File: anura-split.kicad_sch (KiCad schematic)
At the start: 41 parts, among them U1 Nice_Nano_V2

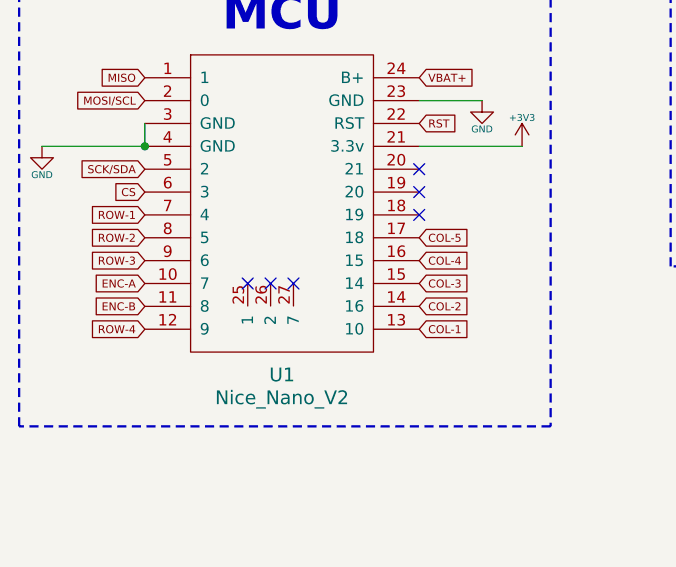
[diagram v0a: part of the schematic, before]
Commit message: lib-anura updates
added and updated variety of symbols in schematic library, to get rid of
dependencies
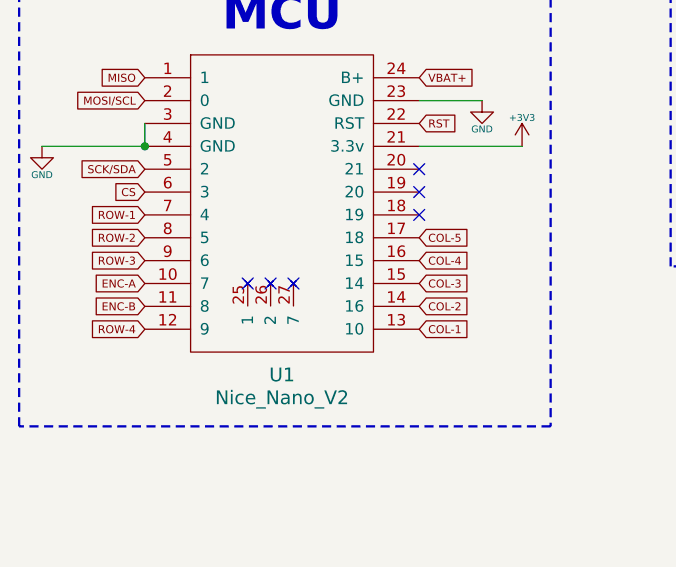
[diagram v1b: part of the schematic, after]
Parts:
- D-1, D-10, D-11, D-12, D-13, D-14, D-15, D-16, D-17, D-18, D-2, D-3, D-4, D-5, D-6, D-7, D-8, D-9: symbol ScottoKeebs:Placeholder_Diode -> lib-anura:Diode_SOD123
- DS-L-1: symbol lib-chungus:Nice!View -> lib-anura:Nice!View
- SW-1, SW-10, SW-11, SW-12, SW-13, SW-14, SW-15, SW-16, SW-17, SW-2, SW-3, SW-4, SW-5, SW-6, SW-7, SW-8, SW-9: symbol ScottoKeebs:Placeholder_Keyswitch -> lib-anura:SW_Push_45_Deg
- SW-BAT-1: symbol Switch:SW_SPDT -> lib-anura:SW_SPDT
- SW-RST-L1: symbol Switch:SW_Push -> lib-anura:SW_Push
- U1: symbol ScottoKeebs:MCU_Nice_Nano_V2 -> lib-anura:MCU_Nice_Nano_V2
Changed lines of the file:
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@@
 	)
 	(symbol
-		(lib_id "ScottoKeebs:Placeholder_Keyswitch")
+		(lib_id "lib-anura:SW_Push_45_Deg")
 		(at 168.275 60.325 0)
 		(unit 1)
@@
 	)
 	(symbol
-		(lib_id "ScottoKeebs:Placeholder_Keyswitch")
+		(lib_id "lib-anura:SW_Push_45_Deg")
 		(at 186.055 79.375 0)
 		(unit 1)
@@
 	)
 	(symbol
-		(lib_id "ScottoKeebs:Placeholder_Diode")
+		(lib_id "lib-anura:Diode_SOD123")
 		(at 224.155 85.725 90)
 		(unit 1)
@@
 	)
 	(symbol
-		(lib_id "ScottoKeebs:Placeholder_Diode")
+		(lib_id "lib-anura:Diode_SOD123")
 		(at 206.375 85.725 90)
 		(unit 1)
@@
 	)
 	(symbol
-		(lib_id "ScottoKeebs:Placeholder_Keyswitch")
+		(lib_id "lib-anura:SW_Push_45_Deg")
 		(at 239.395 79.375 0)
 		(unit 1)
@@
 	)
 	(symbol
-		(lib_id "ScottoKeebs:Placeholder_Keyswitch")
+		(lib_id "lib-anura:SW_Push_45_Deg")
 		(at 221.615 60.325 0)
 		(unit 1)
@@
 	)
 	(symbol
-		(lib_id "ScottoKeebs:Placeholder_Keyswitch")
+		(lib_id "lib-anura:SW_Push_45_Deg")
 		(at 203.835 79.375 0)
 		(unit 1)
@@
 	)
 	(symbol
-		(lib_id "ScottoKeebs:Placeholder_Keyswitch")
+		(lib_id "lib-anura:SW_Push_45_Deg")
 		(at 168.275 79.375 0)
 		(unit 1)
@@
 	)
 	(symbol
-		(lib_id "ScottoKeebs:Placeholder_Diode")
+		(lib_id "lib-anura:Diode_SOD123")
 		(at 188.595 66.675 90)
 		(unit 1)
@@
 	)
 	(symbol
-		(lib_id "ScottoKeebs:Placeholder_Diode")
+		(lib_id "lib-anura:Diode_SOD123")
 		(at 224.155 104.775 90)
 		(unit 1)
@@
 	)
 	(symbol
-		(lib_id "ScottoKeebs:Placeholder_Diode")
+		(lib_id "lib-anura:Diode_SOD123")
 		(at 241.935 85.725 90)
 		(unit 1)
@@
 	)
 	(symbol
-		(lib_id "ScottoKeebs:MCU_Nice_Nano_V2")
+		(lib_id "lib-anura:MCU_Nice_Nano_V2")
 		(at 52.07 44.45 0)
 		(unit 1)
@@
 	)
 	(symbol
-		(lib_id "ScottoKeebs:Placeholder_Diode")
+		(lib_id "lib-anura:Diode_SOD123")
 		(at 241.935 66.675 90)
 		(unit 1)
@@
 	)
 	(symbol
-		(lib_id "ScottoKeebs:Placeholder_Diode")
+		(lib_id "lib-anura:Diode_SOD123")
 		(at 188.595 47.625 90)
 		(unit 1)
@@
 	)
 	(symbol
-		(lib_id "Switch:SW_Push")
+		(lib_id "lib-anura:SW_Push")
 		(at 116.205 74.93 0)
 		(unit 1)
@@
 	)
 	(symbol
-		(lib_id "ScottoKeebs:Placeholder_Diode")
+		(lib_id "lib-anura:Diode_SOD123")
 		(at 206.375 47.625 90)
 		(unit 1)
@@
 	)
 	(symbol
-		(lib_id "ScottoKeebs:Placeholder_Keyswitch")
+		(lib_id "lib-anura:SW_Push_45_Deg")
 		(at 239.395 98.425 0)
 		(unit 1)
@@
 	)
 	(symbol
-		(lib_id "ScottoKeebs:Placeholder_Diode")
+		(lib_id "lib-anura:Diode_SOD123")
 		(at 224.155 47.625 90)
 		(unit 1)
@@
 	)
 	(symbol
-		(lib_id "ScottoKeebs:Placeholder_Keyswitch")
+		(lib_id "lib-anura:SW_Push_45_Deg")
 		(at 221.615 98.425 0)
 		(unit 1)
@@
 	)
 	(symbol
-		(lib_id "ScottoKeebs:Placeholder_Diode")
+		(lib_id "lib-anura:Diode_SOD123")
 		(at 170.815 47.625 90)
 		(unit 1)
@@
 	)
 	(symbol
-		(lib_id "ScottoKeebs:Placeholder_Diode")
+		(lib_id "lib-anura:Diode_SOD123")
 		(at 224.155 66.675 90)
 		(unit 1)
@@
 	)
 	(symbol
-		(lib_id "lib-chungus:Nice!View")
+		(lib_id "lib-anura:Nice!View")
 		(at 121.92 104.14 0)
 		(unit 1)
@@
 	)
 	(symbol
-		(lib_id "ScottoKeebs:Placeholder_Diode")
+		(lib_id "lib-anura:Diode_SOD123")
 		(at 241.935 104.775 90)
 		(unit 1)
@@
 	)
 	(symbol
-		(lib_id "ScottoKeebs:Placeholder_Keyswitch")
+		(lib_id "lib-anura:SW_Push_45_Deg")
 		(at 186.055 60.325 0)
 		(unit 1)
@@
 	)
 	(symbol
-		(lib_id "ScottoKeebs:Placeholder_Keyswitch")
+		(lib_id "lib-anura:SW_Push_45_Deg")
 		(at 239.395 60.325 0)
 		(unit 1)
@@
 	)
 	(symbol
-		(lib_id "ScottoKeebs:Placeholder_Diode")
+		(lib_id "lib-anura:Diode_SOD123")
 		(at 206.375 104.775 90)
 		(unit 1)
@@
 	)
 	(symbol
-		(lib_id "ScottoKeebs:Placeholder_Keyswitch")
+		(lib_id "lib-anura:SW_Push_45_Deg")
 		(at 186.055 41.275 0)
 		(unit 1)
@@
 	)
 	(symbol
-		(lib_id "ScottoKeebs:Placeholder_Keyswitch")
+		(lib_id "lib-anura:SW_Push_45_Deg")
 		(at 203.835 60.325 0)
 		(unit 1)
@@
 	)
 	(symbol
-		(lib_id "ScottoKeebs:Placeholder_Diode")
+		(lib_id "lib-anura:Diode_SOD123")
 		(at 241.935 47.625 90)
 		(unit 1)
@@
 	)
 	(symbol
-		(lib_id "ScottoKeebs:Placeholder_Keyswitch")
+		(lib_id "lib-anura:SW_Push_45_Deg")
 		(at 203.835 41.275 0)
 		(unit 1)
@@
 	)
 	(symbol
-		(lib_id "ScottoKeebs:Placeholder_Keyswitch")
+		(lib_id "lib-anura:SW_Push_45_Deg")
 		(at 168.275 41.275 0)
 		(unit 1)
@@
 	)
 	(symbol
-		(lib_id "ScottoKeebs:Placeholder_Keyswitch")
+		(lib_id "lib-anura:SW_Push_45_Deg")
 		(at 239.395 41.275 0)
 		(unit 1)
@@
 	)
 	(symbol
-		(lib_id "ScottoKeebs:Placeholder_Keyswitch")
+		(lib_id "lib-anura:SW_Push_45_Deg")
 		(at 221.615 41.275 0)
 		(unit 1)
@@
 	)
 	(symbol
-		(lib_id "ScottoKeebs:Placeholder_Diode")
+		(lib_id "lib-anura:Diode_SOD123")
 		(at 206.375 66.675 90)
 		(unit 1)
@@
 	)
 	(symbol
-		(lib_id "ScottoKeebs:Placeholder_Keyswitch")
+		(lib_id "lib-anura:SW_Push_45_Deg")
 		(at 221.615 79.375 0)
 		(unit 1)
@@
 	)
 	(symbol
-		(lib_id "ScottoKeebs:Placeholder_Diode")
+		(lib_id "lib-anura:Diode_SOD123")
 		(at 188.595 85.725 90)
 		(unit 1)
@@
 	)
 	(symbol
-		(lib_id "Switch:SW_SPDT")
+		(lib_id "lib-anura:SW_SPDT")
 		(at 120.65 36.83 0)
 		(unit 1)
@@
 	)
 	(symbol
-		(lib_id "ScottoKeebs:Placeholder_Diode")
+		(lib_id "lib-anura:Diode_SOD123")
 		(at 170.815 85.725 90)
 		(unit 1)
@@
 	)
 	(symbol
-		(lib_id "ScottoKeebs:Placeholder_Diode")
+		(lib_id "lib-anura:Diode_SOD123")
 		(at 170.815 66.675 90)
 		(unit 1)

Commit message: trace routing + silkscreen design
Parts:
- DS-1: renamed from DS-L-1; footprint anura:nice!view -> anura:nice!view_rev2
- renumbered SW-BAT-1 to SW-BAT1, SW-RST-L1 to SW-RST1
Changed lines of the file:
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@@
 		(dnp no)
 		(fields_autoplaced yes)
-		(property "Reference" "SW-RST-L1"
+		(property "Reference" "SW-RST1"
 			(at 116.205 67.31 0)
 			(effects
@@
 			(project "anura-split"
 				(path "/2f4d8bfb-914e-4eb2-88ea-03268c6fd720"
-					(reference "SW-RST-L1")
+					(reference "SW-RST1")
 					(unit 1)
 				)
@@
 		(on_board yes)
 		(dnp no)
-		(property "Reference" "DS-L-1"
+		(property "Reference" "DS-1"
 			(at 121.793 93.218 0)
 			(effects
@@
 			)
 		)
-		(property "Footprint" "anura:nice!view"
+		(property "Footprint" "anura:nice!view_rev2"
 			(at 121.92 104.14 0)
 			(effects
@@
 			(project "anura-split"
 				(path "/2f4d8bfb-914e-4eb2-88ea-03268c6fd720"
-					(reference "DS-L-1")
+					(reference "DS-1")
 					(unit 1)
 				)
@@
 		(on_board yes)
 		(dnp no)
-		(property "Reference" "SW-BAT-1"
+		(property "Reference" "SW-BAT1"
 			(at 120.65 28.702 0)
 			(effects
@@
 			(project "anura-split"
 				(path "/2f4d8bfb-914e-4eb2-88ea-03268c6fd720"
-					(reference "SW-BAT-1")
-					(unit 1)
-				)
+					(reference "SW-BAT1")
+					(unit 1)
+				)

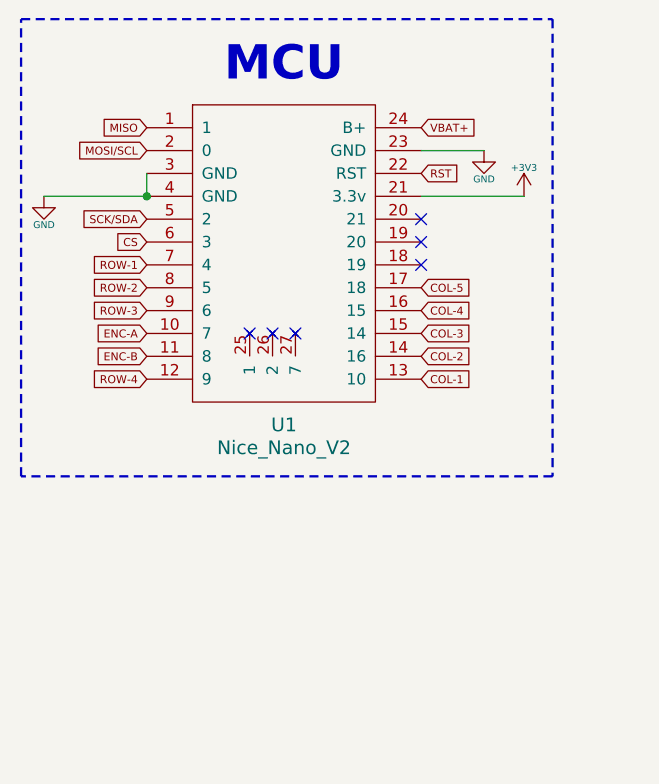
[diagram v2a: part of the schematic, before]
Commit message: routing + schematic changes
mcu nets reorganised to suit trace routing better, and more traces
routed
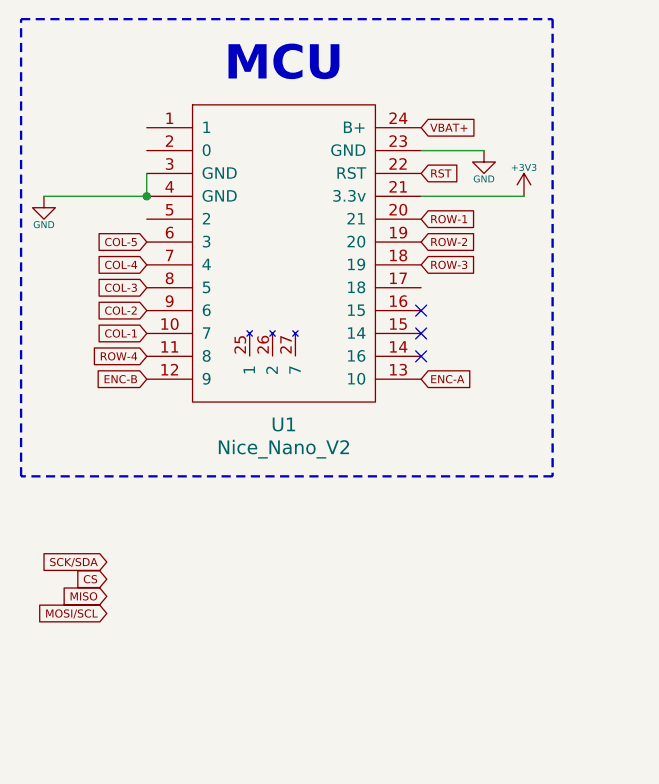
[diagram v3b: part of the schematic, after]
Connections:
- net COL-1: now also U1.10 (7); no longer U1.13 (10)
- net COL-2: now also U1.9 (6); no longer U1.14 (16)
- net COL-3: now also U1.8 (5); no longer U1.15 (14)
- net COL-4: now also U1.7 (4); no longer U1.16 (15)
- net COL-5: now also U1.6 (3); no longer U1.17 (18)
- net CS: no longer U1.6 (3)
- net ENC-A: now also U1.13 (10); no longer U1.10 (7)
- net ENC-B: now also U1.12 (9); no longer U1.11 (8)
- net MISO: no longer U1.1
- net MOSI/SCL: no longer U1.2 (0)
- net ROW-1: now also U1.20 (21); no longer U1.7 (4)
- net ROW-2: now also U1.19 (20); no longer U1.8 (5)
- net ROW-3: now also U1.18 (19); no longer U1.9 (6)
- net ROW-4: now also U1.11 (8); no longer U1.12 (9)
- net SCK/SDA: no longer U1.5 (2)
- no-connect marks 7 -> 4
